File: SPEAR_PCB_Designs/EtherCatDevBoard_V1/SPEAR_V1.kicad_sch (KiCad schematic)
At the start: 32 parts, among them J3 Conn_01x21_Pin, J4 Conn_01x21_Pin, J5 FTSH-107-01-F-DV-K-P-TR, J6 USB_C_Receptacle_USB2.0_16P, SW1 SW_Push, U1 AMS1117-3.3, U2 STM32F446RCTx, U4 USBLC6-2SC6, Y2 16MHz

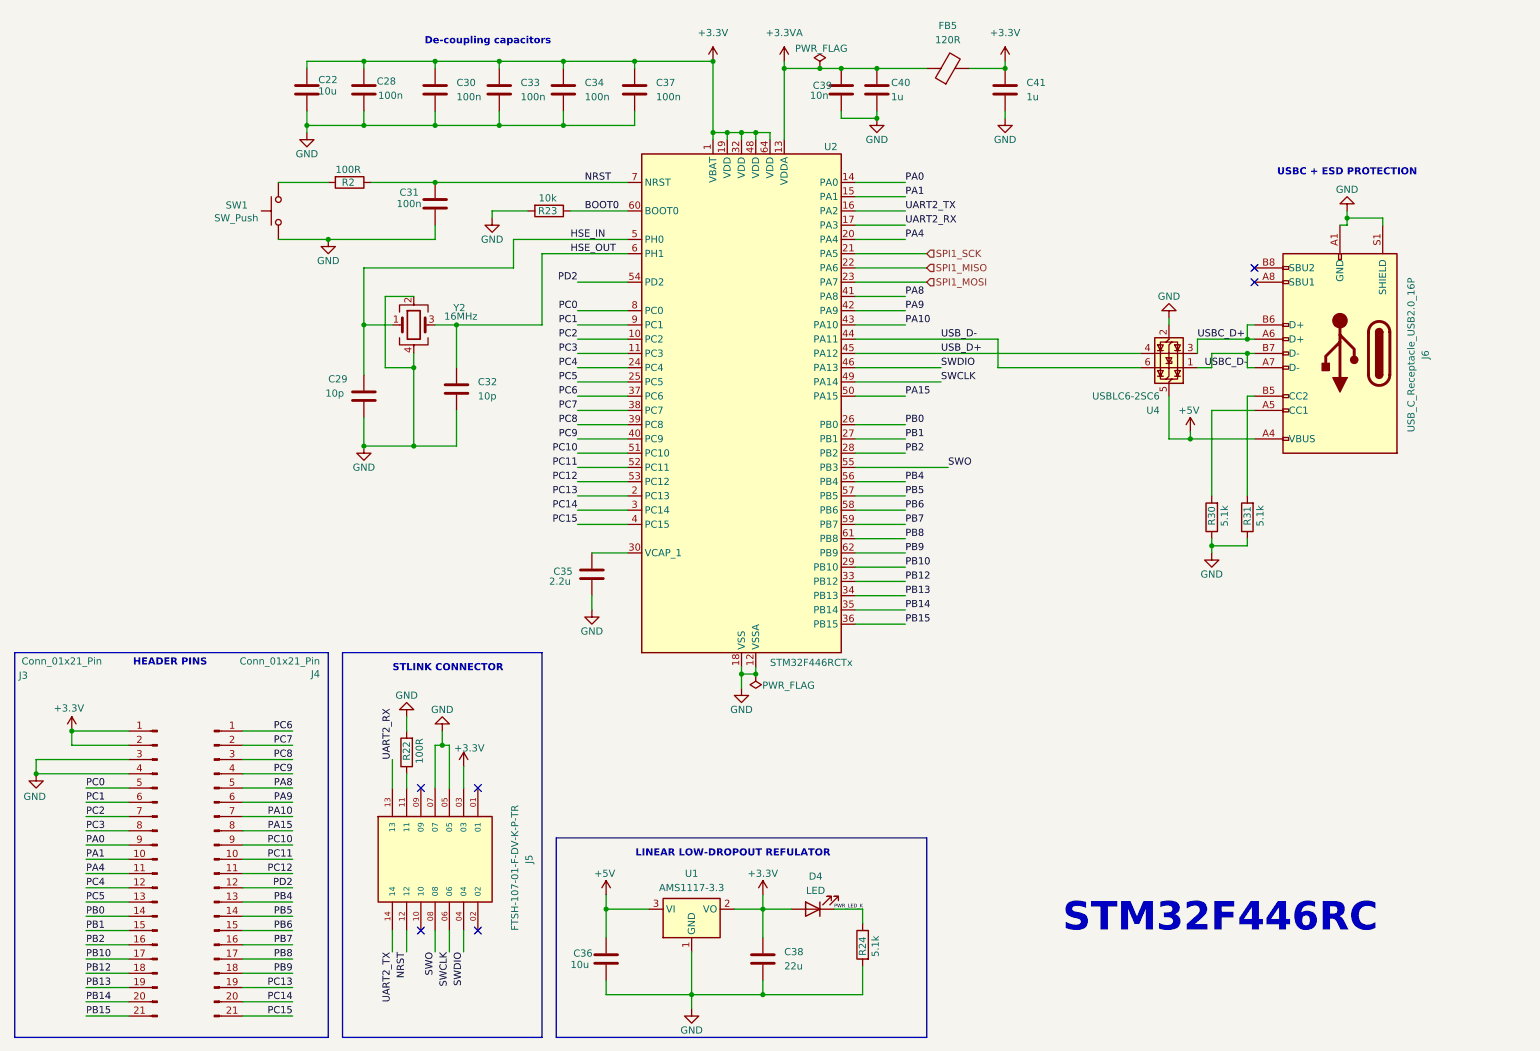
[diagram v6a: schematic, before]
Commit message: Added Lan9252 EtherCAT system to the microcontroller dev board. The schematic is updated, but the pcb layout is still being worked on.
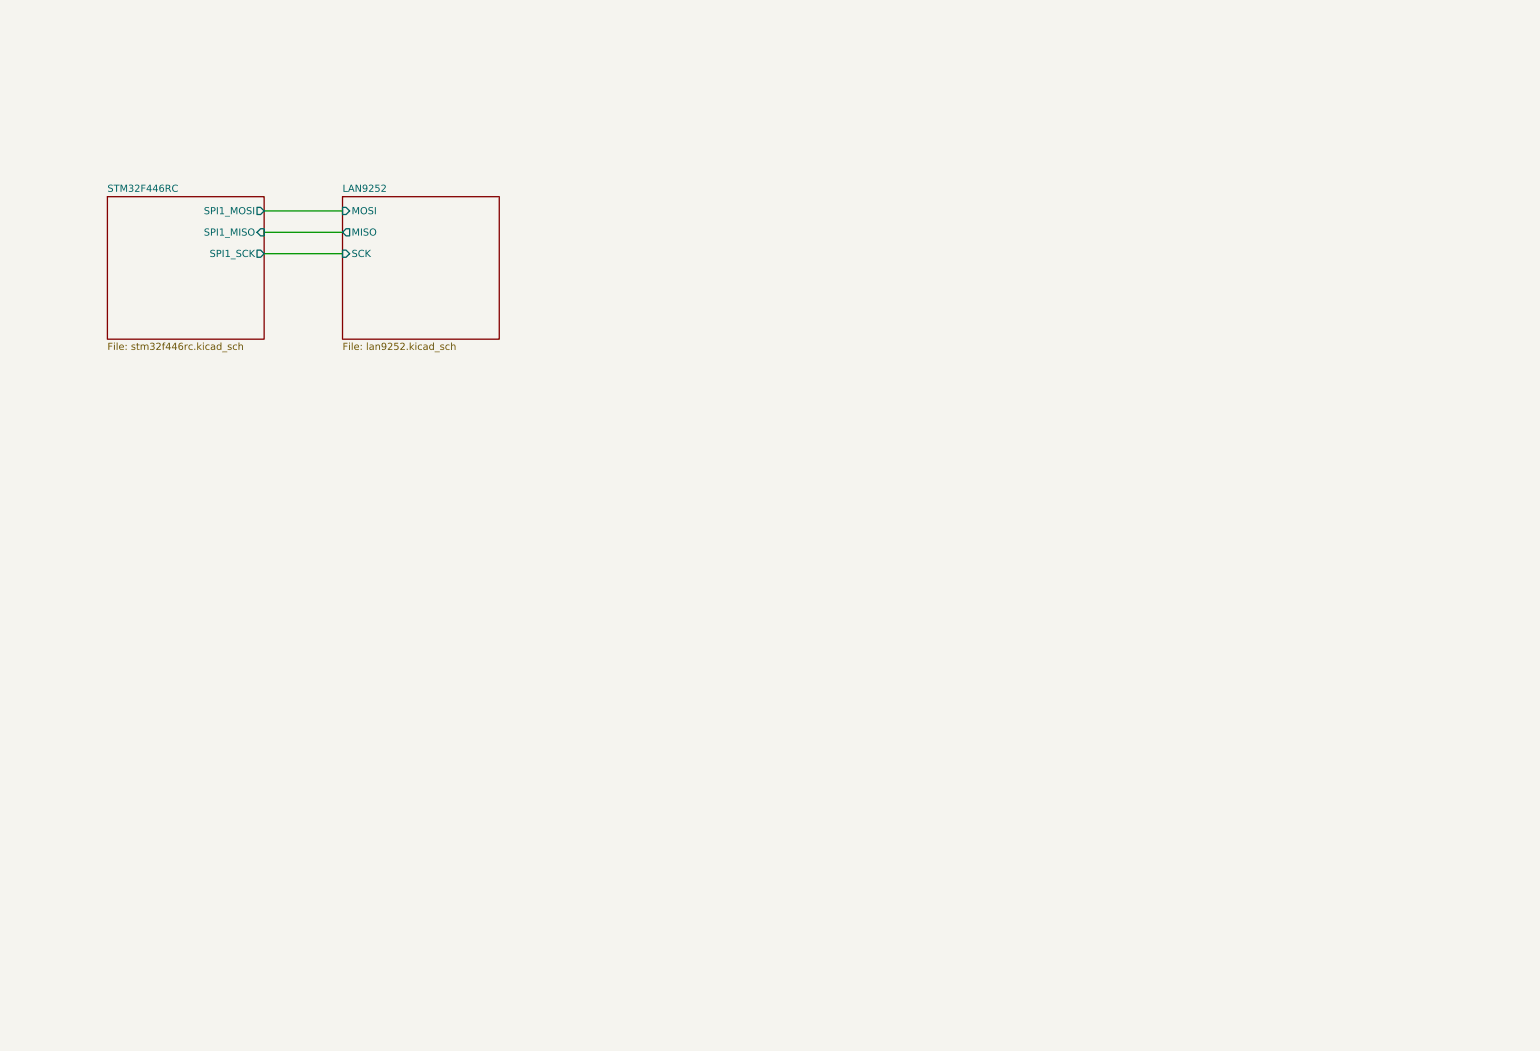
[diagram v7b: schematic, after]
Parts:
- removed C22: 10u, Capacitor_SMD:C_0603_1608Metric, symbol Device:C
- removed C28, C30, C31, C33, C34, C37: 100n, Capacitor_SMD:C_0402_1005Metric, symbol Device:C
- removed C29, C32: 10p, Capacitor_SMD:C_0402_1005Metric, symbol Device:C
- removed C35: 2.2u, Capacitor_SMD:C_0402_1005Metric, symbol Device:C
- removed C36: 10u, Capacitor_SMD:C_0402_1005Metric, symbol Device:C
- removed C38: 22u, Capacitor_SMD:C_0805_2012Metric, symbol Device:C
- removed C39: 10n, Capacitor_SMD:C_0402_1005Metric, symbol Device:C
- removed C40, C41: 1u, Capacitor_SMD:C_0402_1005Metric, symbol Device:C
- removed D4: LED, LED_SMD:LED_0201_0603Metric, symbol Device:LED
- removed FB5: 120R, Inductor_SMD:L_0603_1608Metric, symbol Device:FerriteBead
- removed J3, J4: Conn_01x21_Pin, Connector_PinHeader_2.54mm:PinHeader_1x21_P2.54mm_Vertical, symbol Connector:Conn_01x21_Pin
- removed J5: FTSH-107-01-F-DV-K-P-TR, Library:SAMTEC_FTSH-107-01-F-DV-K-P-TR, symbol FTSH-107-01-F-DV-K-P-TR:FTSH-107-01-F-DV-K-P-TR
- removed J6: USB_C_Receptacle_USB2.0_16P, Connector_USB:USB_C_Receptacle_GCT_USB4105-xx-A_16P_TopMnt_Horizontal, symbol Connector:USB_C_Receptacle_USB2.0_16P
- removed R2, R22: 100R, Resistor_SMD:R_0402_1005Metric, symbol Device:R
- removed R23: 10k, Resistor_SMD:R_0402_1005Metric, symbol Device:R
- removed R24, R30, R31: 5.1k, Resistor_SMD:R_0402_1005Metric, symbol Device:R
- removed SW1: SW_Push, Button_Switch_SMD:SW_Tactile_SPST_NO_Straight_CK_PTS636Sx25SMTRLFS, symbol Switch:SW_Push
- removed U1: AMS1117-3.3, Package_TO_SOT_SMD:SOT-223-3_TabPin2, symbol Regulator_Linear:AMS1117-3.3
- removed U2: STM32F446RCTx, Package_QFP:LQFP-64_10x10mm_P0.5mm, symbol MCU_ST_STM32F4:STM32F446RCTx
- removed U4: USBLC6-2SC6, Package_TO_SOT_SMD:SOT-23-6, symbol Power_Protection:USBLC6-2SC6
- removed Y2: 16MHz, Crystal:Crystal_SMD_3225-4Pin_3.2x2.5mm, symbol Device:Crystal_GND24
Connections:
- no-connect marks 6 -> 0
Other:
- added sheet LAN9252 (lan9252.kicad_sch)
- added sheet STM32F446RC (stm32f446rc.kicad_sch)
- note removed: "De-coupling capacitors"
- note removed: "HEADER PINS"
- note removed: "LINEAR LOW-DROPOUT REFULATOR"
- note removed: "STLINK CONNECTOR"
- note removed: "STM32F446RC"
- note removed: "USBC + ESD PROTECTION"

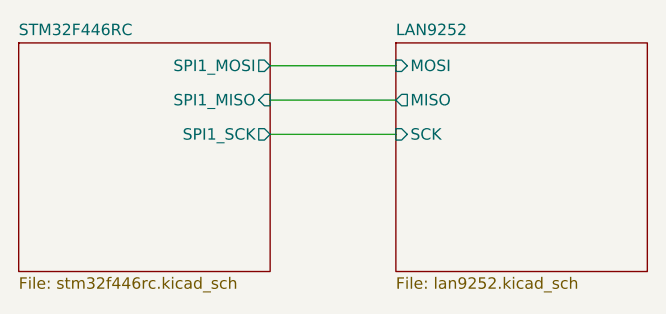
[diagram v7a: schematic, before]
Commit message: Edited schematic to fix problems with Lan9252. Continued work on pcb layout.
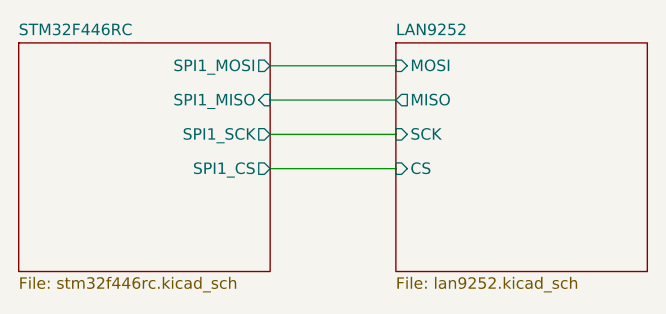
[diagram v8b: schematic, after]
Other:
- sheet LAN9252 ports: added CS; removed none
- sheet STM32F446RC ports: added SPI1_CS; removed none
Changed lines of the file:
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@@
+		)
+	)
+	(wire
+		(pts
+			(xy 57.15 59.69) (xy 71.12 59.69)
+		)
+		(stroke
+			(width 0)
+			(type default)
 		)
 	)
@@
 		(pin "SPI1_SCK" output
 			(at 57.15 55.88 0)
+			(effects
+				(font
+					(size 1.27 1.27)
+				)
+				(justify right)
+			)
+		)
+		(pin "SPI1_CS" output
+			(at 57.15 59.69 0)
 			(effects
 				(font
@@
 			(effects
 				(font
+					(size 1.27 1.27)
+				)
+				(justify left)
+			)
+		)
+		(pin "CS" input
+			(at 71.12 59.69 180)
+			(effects
+				(font
